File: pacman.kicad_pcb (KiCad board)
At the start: 2 copper layers, 227.4 x 78 mm, 148 parts, among them J1 RESET, J2 BOOT, SW1 MX_LED, SW10 MX_LED, SW11 MX_LED, SW12 MX_LED, SW13 MX_LED, SW14 MX_LED, SW15 MX_LED, SW16 MX_LED, SW17 MX_LED, SW18 MX_LED, SW19 MX_LED, SW2 MX_LED, SW20 MX_LED, SW21 MX_LED, SW22 MX_LED, SW23 MX_LED, SW24 MX_LED, SW25 MX_LED, SW26 MX_LED, SW27 MX_LED, SW28 MX_LED, SW29 MX_LED, SW3 MX_LED, SW30 MX_LED, SW31 MX_LED, SW32 MX_LED, SW33 MX_LED, SW34 MX_LED, SW35 MX_LED, SW36 MX_LED, SW37 MX_LED, SW38 MX_LED, SW39 MX_LED, SW4 MX_LED, SW40 MX_LED, SW41 MX_LED, SW42_2 MX_LED, SW44 MX_LED, SW45 MX_LED, SW46 MX_LED, SW47 MX_LED, SW48 MX_LED, SW5 MX_LED, SW6 MX_LED, SW7 MX_LED, SW8 MX_LED, SW9 MX_LED, U1 NCP1117-3.3_SOT223, U2 RP2040, U3 W25Q128JVS, Y1 12MHz

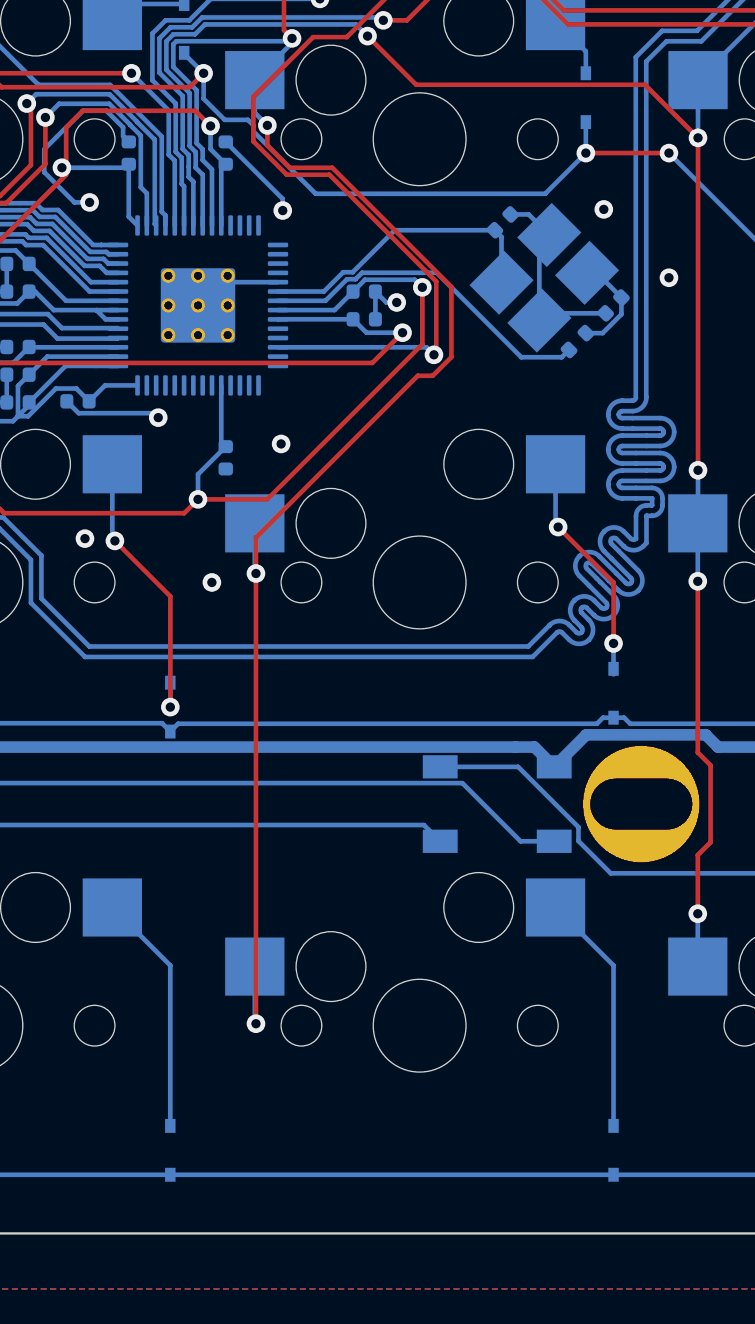
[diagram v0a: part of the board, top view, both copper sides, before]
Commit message: Fix unconnected rows
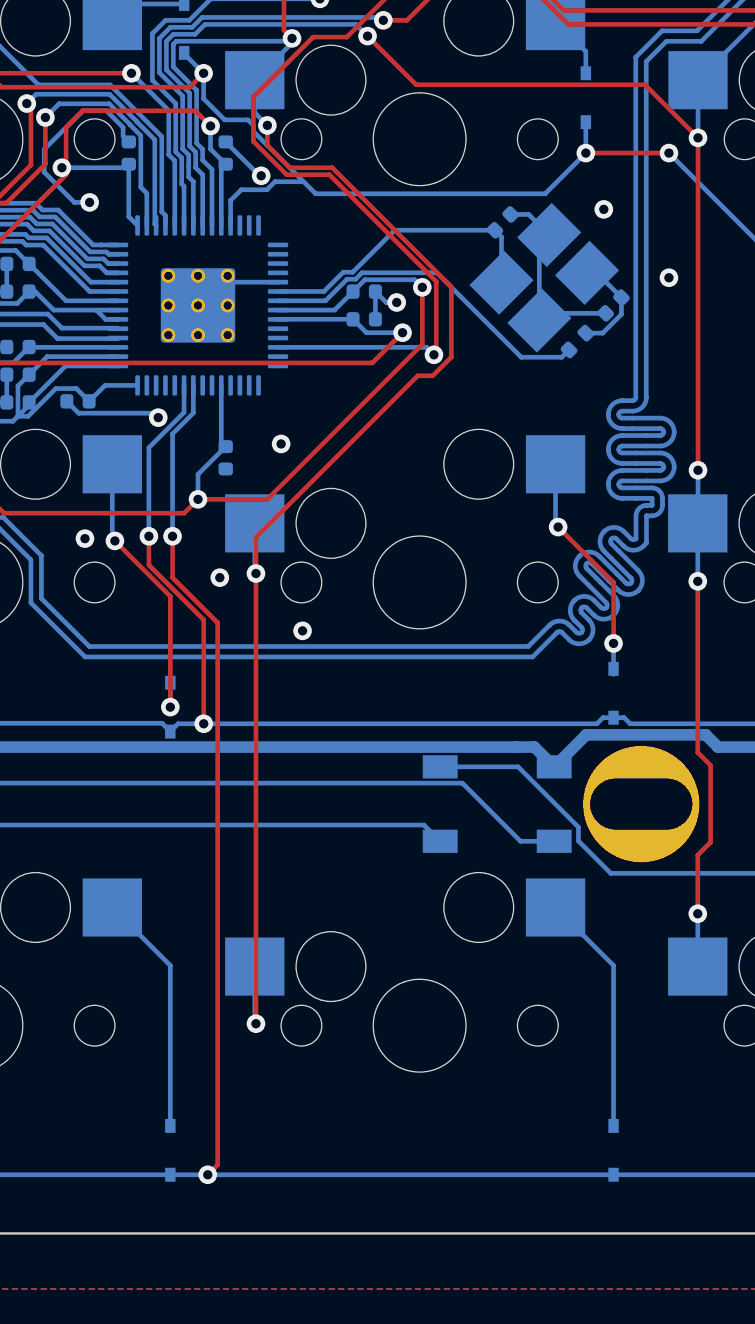
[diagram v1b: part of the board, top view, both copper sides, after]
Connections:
- U2 pad 11: unconnected-(U2-Pad11) -> row1
- U2 pad 36: unconnected-(U2-Pad36) -> row3
- U2 pad 37: unconnected-(U2-Pad37) -> row2
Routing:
- net row3: track 195.0 -> 230.3 mm, vias 0 -> 2
- net row2: track 195.1 -> 211.2 mm, vias 0 -> 2
- net row1: track 206.8 -> 211.4 mm
- net GND: track 418.3 -> 416.4 mm, vias 31 -> 32

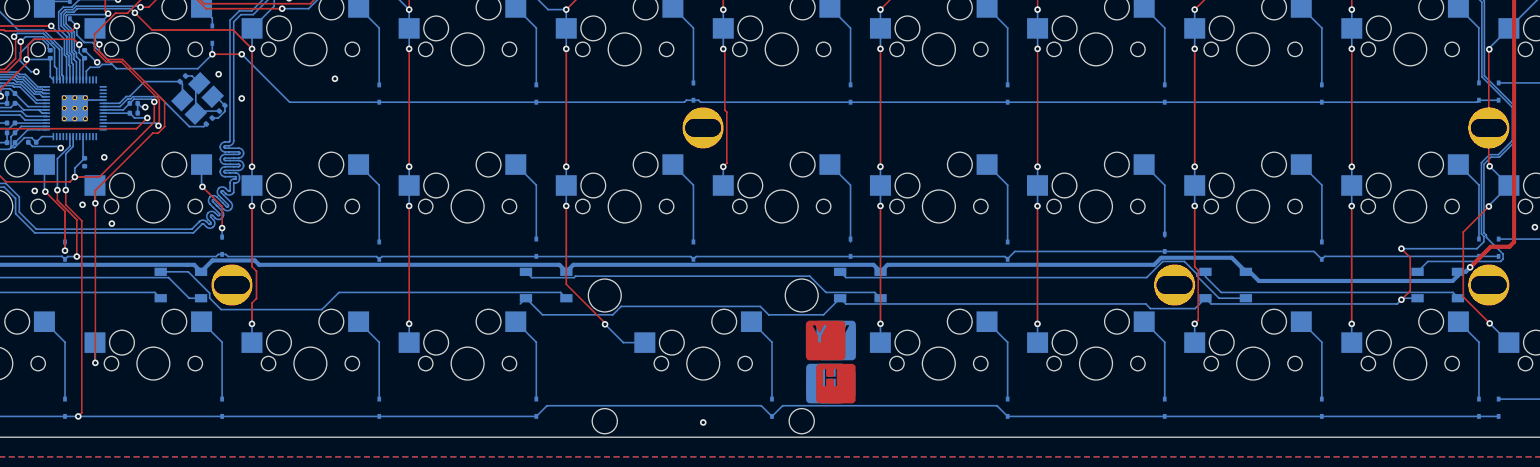
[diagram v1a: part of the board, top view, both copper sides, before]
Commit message: Fix unconnected Column
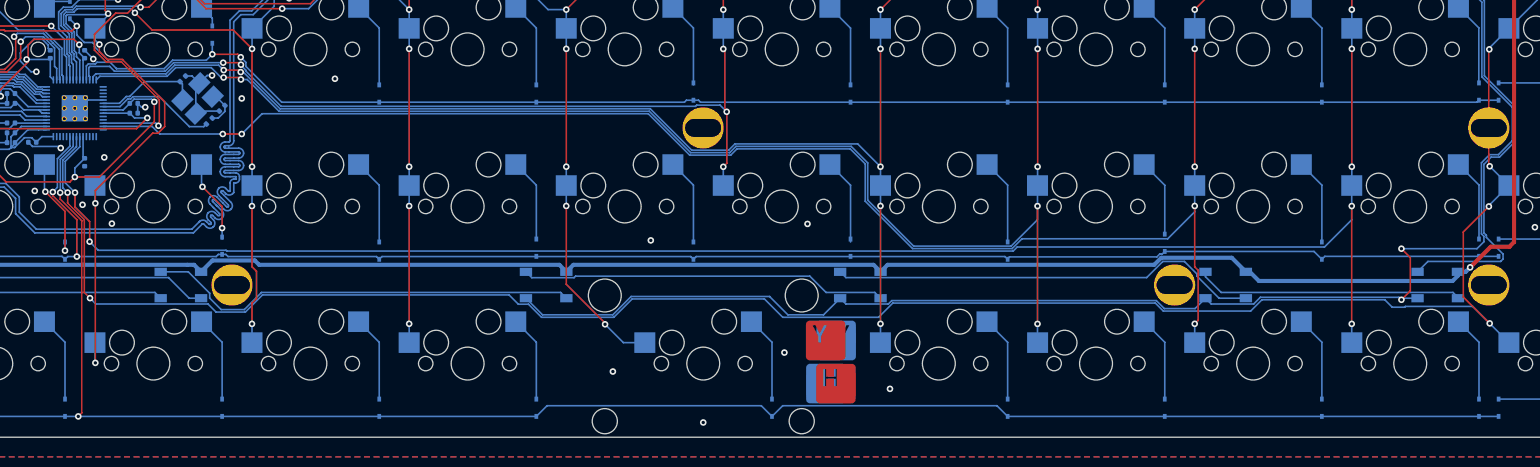
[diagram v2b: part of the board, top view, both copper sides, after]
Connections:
- U2 pad 12: unconnected-(U2-Pad12) -> col6
- U2 pad 13: unconnected-(U2-Pad13) -> col7
- U2 pad 14: unconnected-(U2-Pad14) -> col8
- U2 pad 27: unconnected-(U2-Pad27) -> col9
- U2 pad 34: unconnected-(U2-Pad34) -> col10
- U2 pad 35: unconnected-(U2-Pad35) -> col11
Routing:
- net col11: track 66.8 -> 265.7 mm, vias 4 -> 6
- net col10: track 57.2 -> 228.7 mm, vias 6 -> 8
- net col9: track 60.6 -> 207.1 mm, vias 6 -> 8
- net col8: track 57.2 -> 187.1 mm, vias 6 -> 8
- net col7: track 59.9 -> 162.1 mm, vias 6 -> 8
- net col6: track 38.5 -> 121.1 mm, vias 4 -> 7
- net GND: track 416.4 -> 418.3 mm, vias 32 -> 37
- net row3: track 230.3 -> 230.9 mm

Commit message: Add Encoder
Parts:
- added SW42: RotaryEncoder_Switch, Keebio-Parts:RotaryEncoder_EC11, F.Cu at (27.4, 27.4)
- added SW43: RotaryEncoder_Switch, Keebio-Parts:RotaryEncoder_EC11, F.Cu at (236.9, 27.4)
- moved C14 26.9 mm to (45.8, 21.4)
- moved U1 16.8 mm to (40.5, 22.6)
- moved C15 13.0 mm to (38.1, 27.4)
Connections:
- U2 pad 17: unconnected-(U2-Pad17) -> ENC_1_A
- U2 pad 18: unconnected-(U2-Pad18) -> ENC_1_B
- U2 pad 31: unconnected-(U2-Pad31) -> ENC_0_B
- U2 pad 32: unconnected-(U2-Pad32) -> ENC_0_A
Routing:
- net ENC_1_B: track 0.00 -> 190.6 mm, vias 0 -> 4
- net ENC_1_A: track 0.00 -> 190.1 mm, vias 0 -> 4
- net ENC_0_B: track 0.00 -> 92.4 mm, vias 0 -> 2
- net ENC_0_A: track 0.00 -> 87.9 mm, vias 0 -> 2
- net +3V3: track 177.1 -> 198.5 mm
- net col11: track 265.7 -> 285.3 mm
- net GND: track 418.3 -> 431.8 mm, vias 37 -> 42
- net col0: track 98.4 -> 104.9 mm
- net Net-(D1-A): track 4.22 -> 8.36 mm
- net col3: track 93.6 -> 96.0 mm
- net VBUS: track 502.8 -> 501.2 mm
- net col2: track 79.8 -> 81.4 mm
- net Net-(D12-A): track 24.7 -> 26.2 mm
- net /XOUT: track 14.6 -> 16.0 mm
- net row0: track 259.0 -> 257.9 mm
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
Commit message: fix fill
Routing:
- net Net-(D31-A): track 10.4 -> 13.6 mm
- net col9: track 207.1 -> 209.4 mm
- net col8: track 187.1 -> 189.4 mm
